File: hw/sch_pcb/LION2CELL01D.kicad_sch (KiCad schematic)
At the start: 100 parts, among them J1 JUMP_4X2, J10 JUMP_2x1, J11 JUMP_2x1, J12 JUMP_2x1, J13 JUMP_4X2, J14 JUMP_2x1, J15 CONN_2, J2 JUMP_2x1, J3 JUMP_2x1, J4 JUMP2_2x1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

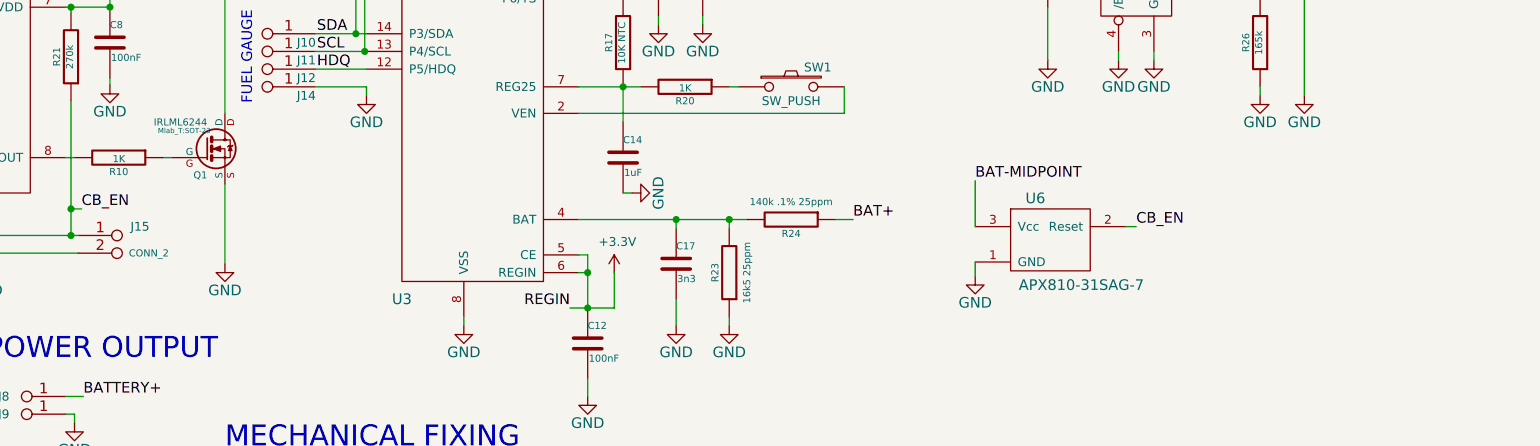
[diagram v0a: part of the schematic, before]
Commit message: Update documentation. Improve schematic (title block, texts) Regenerate PDF export.
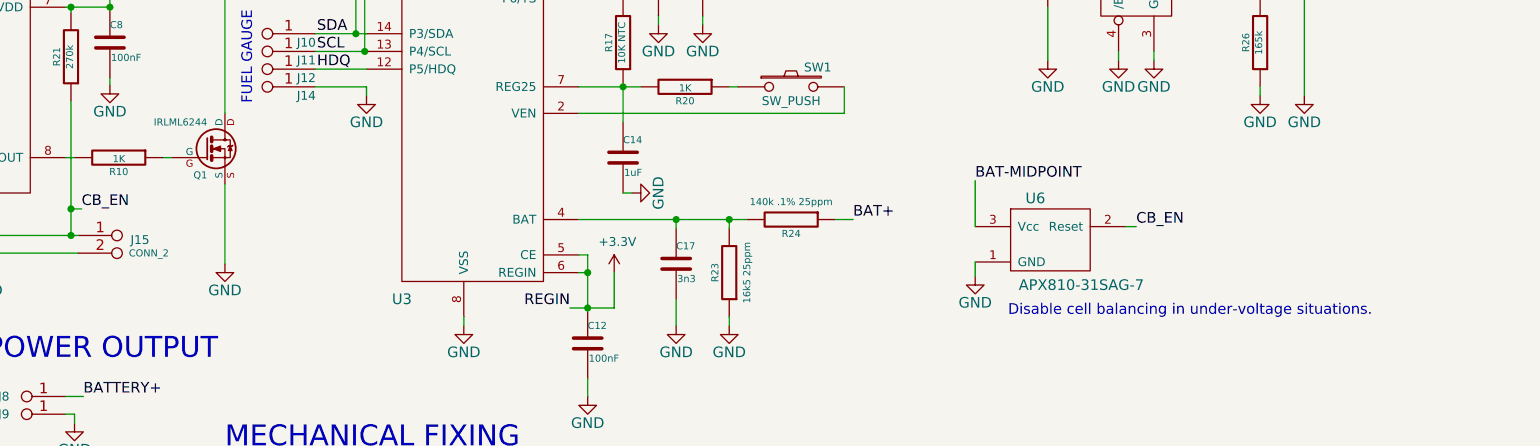
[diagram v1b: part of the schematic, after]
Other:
- note added: "Disable cell balancing in under-voltage situations."
- company: (none) -> jacho <jacho@mlab.cz>
- title: (none) -> Li-ion battery managment

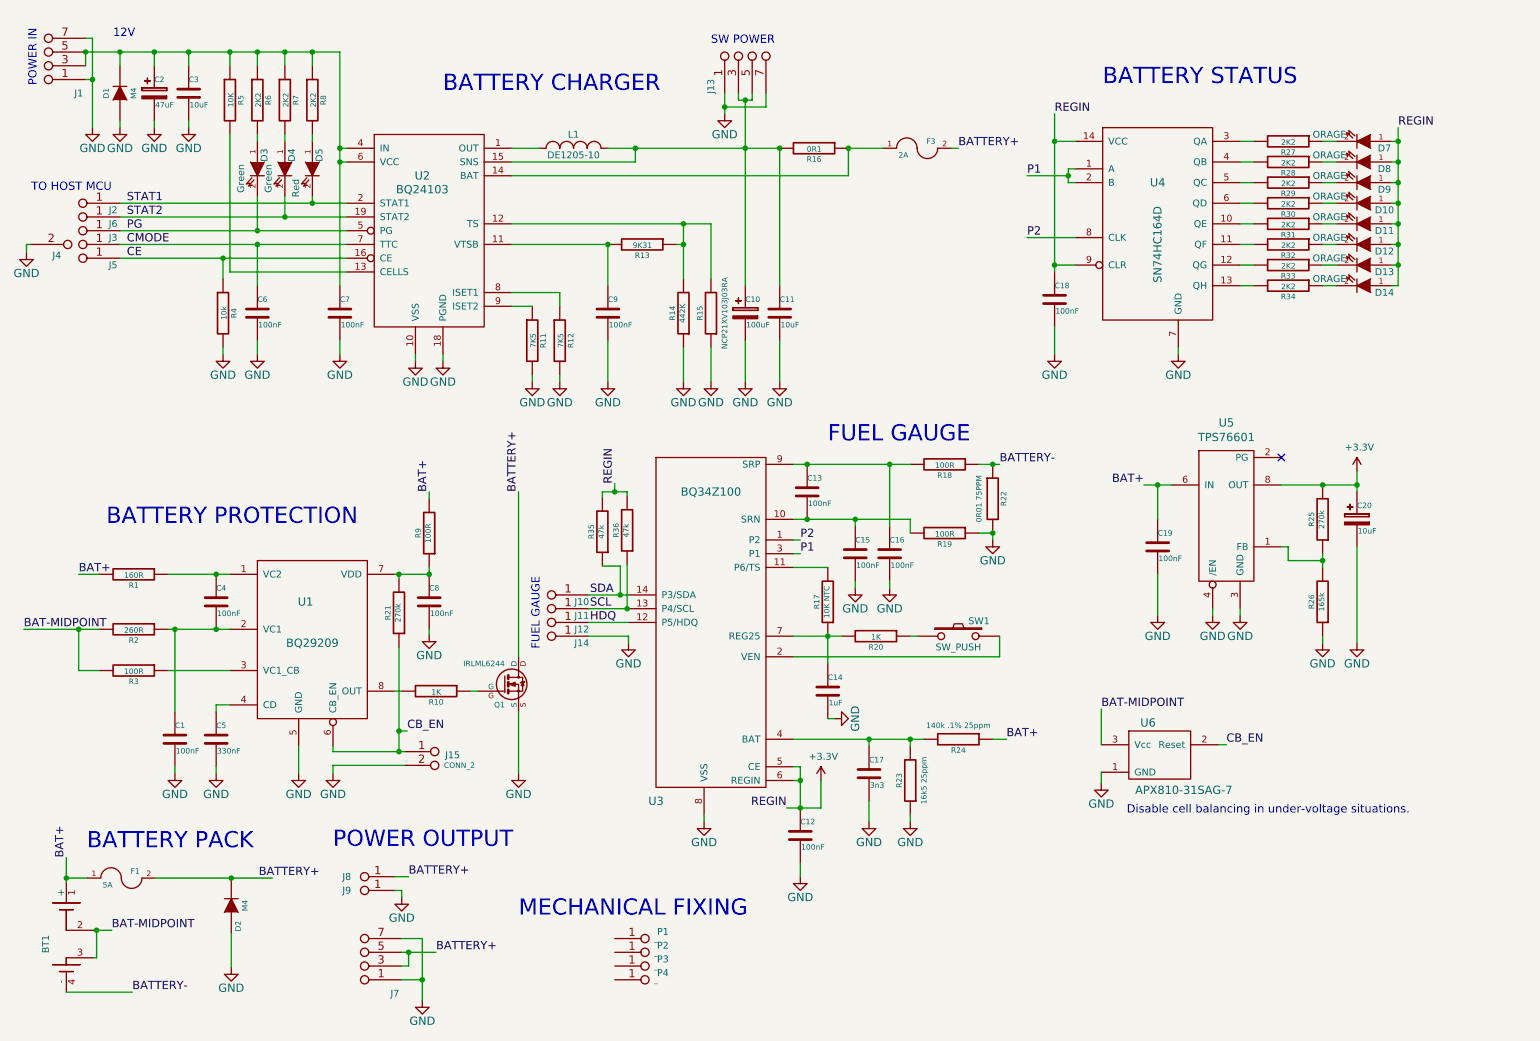
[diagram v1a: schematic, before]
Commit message: Update title block and assets submodule.
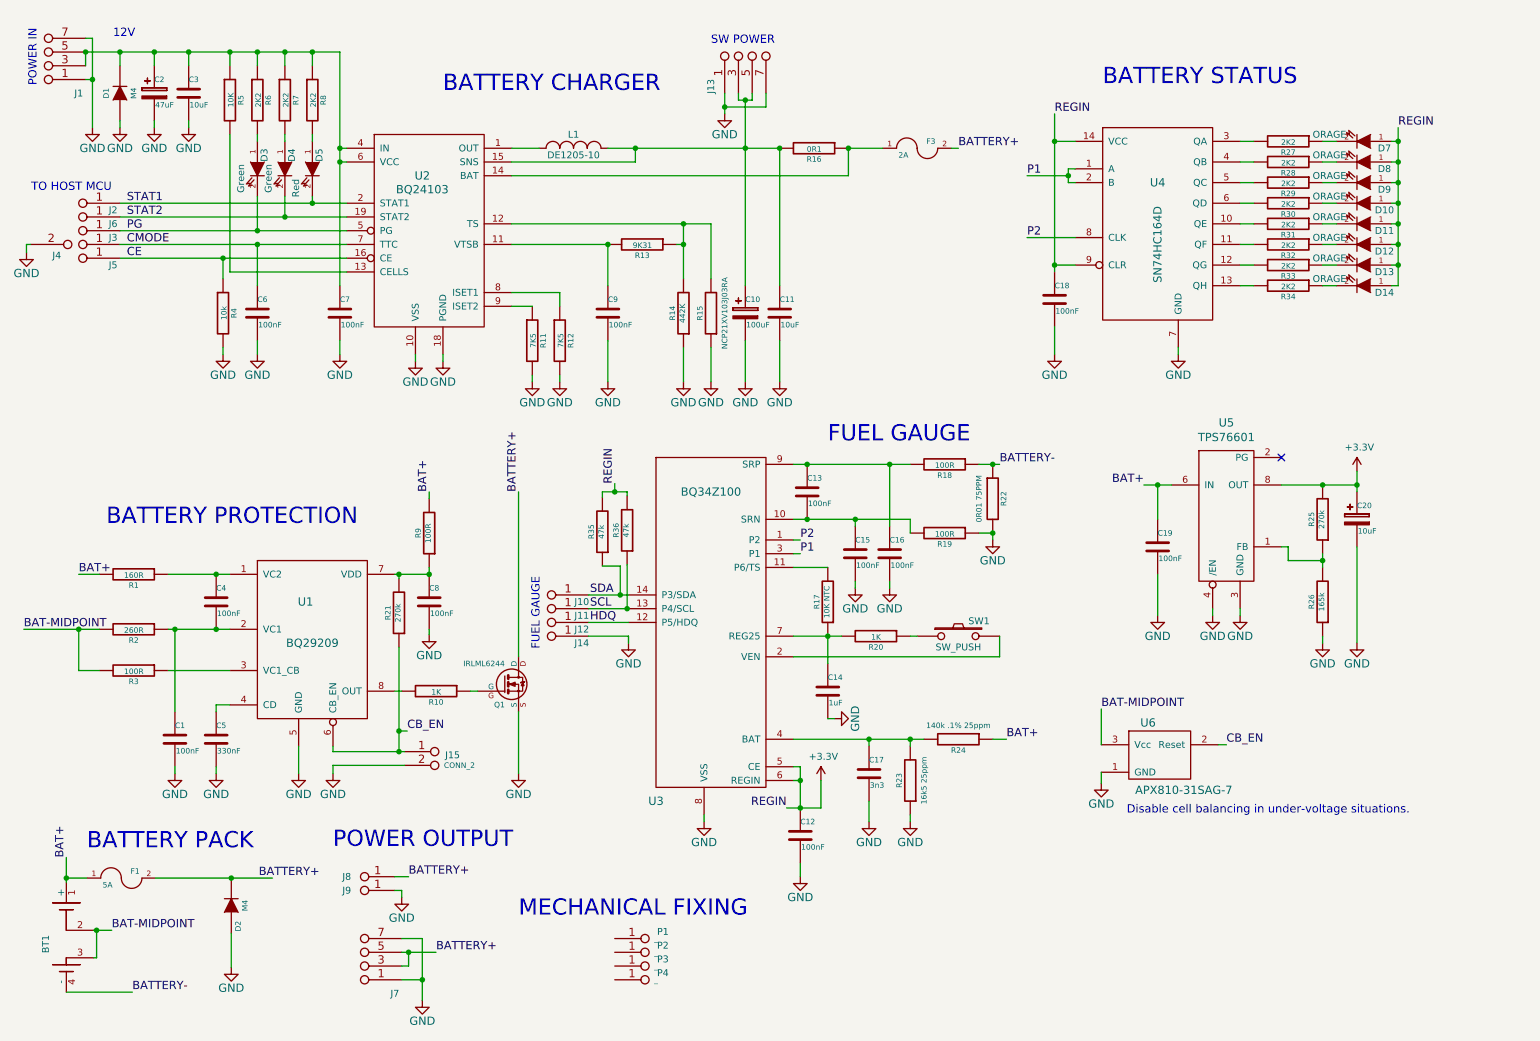
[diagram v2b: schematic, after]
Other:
- title: Li-ion battery managment -> LION2CELL01D
